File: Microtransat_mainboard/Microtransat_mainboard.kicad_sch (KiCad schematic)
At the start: 17 parts, among them IC1 HT7833, U1 LM2596S-5, U10 RC_Reciever, U5 SD Card Module, U7 LoRa Module

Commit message: Added AS5600 mockup
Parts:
- removed U7: LoRa Module, symbol Microtransat:LoRa Module
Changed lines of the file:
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@@
-		)
-	)
-	(label "RX1"
-		(at 160.02 67.31 180)
-		(effects
-			(font
-				(size 1.27 1.27)
-			)
-			(justify right bottom)
 		)
 	)
@@
 		)
 	)
-	(label "TX1"
-		(at 160.02 69.85 180)
-		(effects
-			(font
-				(size 1.27 1.27)
-			)
-			(justify right bottom)
-		)
-	)
 	(label "3V3"
 		(at 70.485 114.3 180)
@@
 			)
 			(justify left bottom)
-		)
-	)
-	(label "GND"
-		(at 160.02 64.77 180)
-		(effects
-			(font
-				(size 1.27 1.27)
-			)
-			(justify right bottom)
-		)
-	)
-	(label "5V"
-		(at 160.02 62.23 180)
-		(effects
-			(font
-				(size 1.27 1.27)
-			)
-			(justify right bottom)
 		)
 	)
@@
 					(unit 1)
 				)
-			)
-		)
-	)
-	(symbol
-		(lib_id "Microtransat:LoRa Module")
-		(at 168.275 57.15 0)
-		(unit 1)
-		(exclude_from_sim no)
-		(in_bom yes)
-		(on_board yes)
-		(dnp no)
-		(property "Reference" "U7"
-			(at 166.116 55.372 0)
-			(effects
-				(font
-					(size 1.27 1.27)
-				)
-				(justify left)
-			)
-		)
-		(property "Value" "LoRa Module"
-			(at 161.29 57.658 0)
-			(effects
-				(font
-					(size 1.27 1.27)
-				)
-				(justify left)
-			)
-		)
-		(property "Footprint" ""
-			(at 168.275 57.15 0)
-			(effects
-				(font
-					(size 1.27 1.27)
-				)
-				(hide yes)
-			)
-		)
-		(property "Datasheet" ""
-			(at 168.275 57.15 0)
-			(effects
-				(font
-					(size 1.27 1.27)
-				)
-				(hide yes)
-			)
-		)
-		(property "Description" ""
-			(at 168.275 57.15 0)
-			(effects
-				(font
-					(size 1.27 1.27)
-				)
-				(hide yes)
-			)
-		)
-		(pin "1"
-		)
-		(pin "2"
-		)
-		(pin "3"
-		)
-		(pin "4"
-		)
-		(instances
-			(project "Microtransat_mainboard"
-				(path "/89914625-be83-416e-bb0d-b792f59b4aa6"
-					(reference "U7")
-					(unit 1)
-				)

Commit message: Some adjustments
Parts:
- removed C_in1: 680 µF, symbol Device:C_Polarized
- removed C_out1: 220 µF, symbol Device:C_Polarized
- removed D3: 1N5824, Diode_THT:D_DO-201AD_P15.24mm_Horizontal, symbol Diode:1N5820
- removed L1: 33 µH, symbol Device:L
- added J1: Conn_01x03, symbol Connector_Generic:Conn_01x03
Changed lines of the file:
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@@
-	)
-	(junction
-		(at 139.7 40.64)
-		(diameter 0)
-		(color 0 0 0 0)
 	)
 	(junction
@@
 	(wire
 		(pts
-			(xy 139.7 40.64) (xy 152.4 40.64)
+			(xy 123.19 40.64) (xy 152.4 40.64)
 		)
 		(stroke
@@
 		(pts
 			(xy 68.58 43.18) (xy 68.58 40.64)
-		)
-		(stroke
-			(width 0)
-			(type default)
-		)
-	)
-	(wire
-		(pts
-			(xy 139.7 40.64) (xy 123.19 40.64)
 		)
 		(stroke
@@
 			)
 			(justify left bottom)
-		)
-	)
-	(symbol
-		(lib_id "Device:L")
-		(at 146.05 31.75 90)
-		(unit 1)
-		(exclude_from_sim no)
-		(in_bom yes)
-		(on_board yes)
-		(dnp no)
-		(fields_autoplaced yes)
-		(property "Reference" "L1"
-			(at 146.05 26.67 90)
-			(effects
-				(font
-					(size 1.27 1.27)
-				)
-			)
-		)
-		(property "Value" "33 µH"
-			(at 146.05 29.21 90)
-			(effects
-				(font
-					(size 1.27 1.27)
-				)
-			)
-		)
-		(property "Footprint" ""
-			(at 146.05 31.75 0)
-			(effects
-				(font
-					(size 1.27 1.27)
-				)
-				(hide yes)
-			)
-		)
-		(property "Datasheet" "~"
-			(at 146.05 31.75 0)
-			(effects
-				(font
-					(size 1.27 1.27)
-				)
-				(hide yes)
-			)
-		)
-		(property "Description" "Inductor"
-			(at 146.05 31.75 0)
-			(effects
-				(font
-					(size 1.27 1.27)
-				)
-				(hide yes)
-			)
-		)
-		(pin "2"
-		)
-		(pin "1"
-		)
-		(instances
-			(project "Microtransat_mainboard"
-				(path "/89914625-be83-416e-bb0d-b792f59b4aa6"
-					(reference "L1")
-					(unit 1)
-				)
-			)
-		)
-	)
-	(symbol
-		(lib_id "Diode:1N5820")
-		(at 139.7 36.83 270)
-		(unit 1)
-		(exclude_from_sim no)
-		(in_bom yes)
-		(on_board yes)
-		(dnp no)
-		(fields_autoplaced yes)
-		(property "Reference" "D3"
-			(at 142.24 35.2424 90)
-			(effects
-				(font
-					(size 1.27 1.27)
-				)
-				(justify left)
-			)
-		)
-		(property "Value" "1N5824"
-			(at 142.24 37.7824 90)
-			(effects
-				(font
-					(size 1.27 1.27)
-				)
-				(justify left)
-			)
-		)
-		(property "Footprint" "Diode_THT:D_DO-201AD_P15.24mm_Horizontal"
-			(at 135.255 36.83 0)
-			(effects
-				(font
-					(size 1.27 1.27)
-				)
-				(hide yes)
-			)
-		)
-		(property "Datasheet" "http://www.vishay.com/docs/88526/1n5820.pdf"
-			(at 139.7 36.83 0)
-			(effects
-				(font
-					(size 1.27 1.27)
-				)
-				(hide yes)
-			)
-		)
-		(property "Description" ""
-			(at 139.7 36.83 0)
-			(effects
-				(font
-					(size 1.27 1.27)
-				)
-				(hide yes)
-			)
-		)
-		(pin "1"
-		)
-		(pin "2"
-		)
-		(instances
-			(project "Microtransat_mainboard"
-				(path "/89914625-be83-416e-bb0d-b792f59b4aa6"
-					(reference "D3")
-					(unit 1)
-				)
-			)
 		)
 	)
@@
 	)
 	(symbol
+		(lib_id "Connector_Generic:Conn_01x03")
+		(at 203.2 62.23 0)
+		(unit 1)
+		(exclude_from_sim no)
+		(in_bom yes)
+		(on_board yes)
+		(dnp no)
+		(fields_autoplaced yes)
+		(property "Reference" "J1"
+			(at 205.74 60.9599 0)
+			(effects
+				(font
+					(size 1.27 1.27)
+				)
+				(justify left)
+			)
+		)
+		(property "Value" "Conn_01x03"
+			(at 205.74 63.4999 0)
+			(effects
+				(font
+					(size 1.27 1.27)
+				)
+				(justify left)
+			)
+		)
+		(property "Footprint" ""
+			(at 203.2 62.23 0)
+			(effects
+				(font
+					(size 1.27 1.27)
+				)
+				(hide yes)
+			)
+		)
+		(property "Datasheet" "~"
+			(at 203.2 62.23 0)
+			(effects
+				(font
+					(size 1.27 1.27)
+				)
+				(hide yes)
+			)
+		)
+		(property "Description" "Generic connector, single row, 01x03, script generated (kicad-library-utils/schlib/autogen/connector/)"
+			(at 203.2 62.23 0)
+			(effects
+				(font
+					(size 1.27 1.27)
+				)
+				(hide yes)
+			)
+		)
+		(pin "2"
+		)
+		(pin "1"
+		)
+		(pin "3"
+		)
+		(instances
+			(project ""
+				(path "/89914625-be83-416e-bb0d-b792f59b4aa6"
+					(reference "J1")
+					(unit 1)
+				)
+			)
+		)
+	)
+	(symbol
 		(lib_id "power:+12V")
 		(at 35.56 72.39 0)
@@
 	)
 	(symbol
-		(lib_id "Device:C_Polarized")
-		(at 104.14 33.02 0)
-		(unit 1)
-		(exclude_from_sim no)
-		(in_bom yes)
-		(on_board yes)
-		(dnp no)
-		(property "Reference" "C_in1"
-			(at 95.758 32.004 0)
-			(effects
-				(font
-					(size 1.27 1.27)
-				)
-				(justify left)
-			)
-		)
-		(property "Value" "680 µF"
-			(at 94.488 34.036 0)
-			(effects
-				(font
-					(size 1.27 1.27)
-				)
-				(justify left)
-			)
-		)
-		(property "Footprint" ""
-			(at 105.1052 36.83 0)
-			(effects
-				(font
-					(size 1.27 1.27)
-				)
-				(hide yes)
-			)
-		)
-		(property "Datasheet" "~"
-			(at 104.14 33.02 0)
-			(effects
-				(font
-					(size 1.27 1.27)
-				)
-				(hide yes)
-			)
-		)
-		(property "Description" "Polarized capacitor"
-			(at 104.14 33.02 0)
-			(effects
-				(font
-					(size 1.27 1.27)
-				)
-				(hide yes)
-			)
-		)
-		(pin "2"
-		)
-		(pin "1"
-		)
-		(instances
-			(project "Microtransat_mainboard"
-				(path "/89914625-be83-416e-bb0d-b792f59b4aa6"
-					(reference "C_in1")
-					(unit 1)
-				)
-			)
-		)
-	)
-	(symbol
 		(lib_id "Microtransat:SD Card Module")
 		(at 78.74 115.57 0)
@@
 					(unit 1)
 				)
-			)
-		)
-	)
-	(symbol
-		(lib_id "Device:C_Polarized")
-		(at 152.4 36.83 0)
-		(unit 1)
-		(exclude_from_sim no)
-		(in_bom yes)
-		(on_board yes)
-		(dnp no)
-		(property "Reference" "C_out1"
-			(at 155.702 35.814 0)
-			(effects
-				(font
-					(size 1.27 1.27)
-				)
-				(justify left)
-			)
-		)
-		(property "Value" "220 µF"
-			(at 155.702 37.846 0)
-			(effects
-				(font
-					(size 1.27 1.27)
-				)
-				(justify left)
-			)
-		)
-		(property "Footprint" ""
-			(at 153.3652 40.64 0)
-			(effects
-				(font
-					(size 1.27 1.27)
-				)
-				(hide yes)
-			)
-		)
-		(property "Datasheet" "~"
-			(at 152.4 36.83 0)
-			(effects
-				(font
-					(size 1.27 1.27)
-				)
-				(hide yes)
-			)
-		)
-		(property "Description" "Polarized capacitor"
-			(at 152.4 36.83 0)
-			(effects
-				(font
-					(size 1.27 1.27)
-				)
-				(hide yes)
-			)
-		)
-		(pin "2"
-		)
-		(pin "1"
-		)
-		(instances
-			(project "Microtransat_mainboard"
-				(path "/89914625-be83-416e-bb0d-b792f59b4aa6"
-					(reference "C_out1")
-					(unit 1)
-				)

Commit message: Moved symbol and footprint into libraries folder
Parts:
- U5: footprint (none) -> Adafruit 254:Adafruit_254
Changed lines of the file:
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@@
 			)
 		)
-		(property "Footprint" ""
+		(property "Footprint" "Adafruit 254:Adafruit_254"
 			(at 78.74 115.57 0)
 			(effects

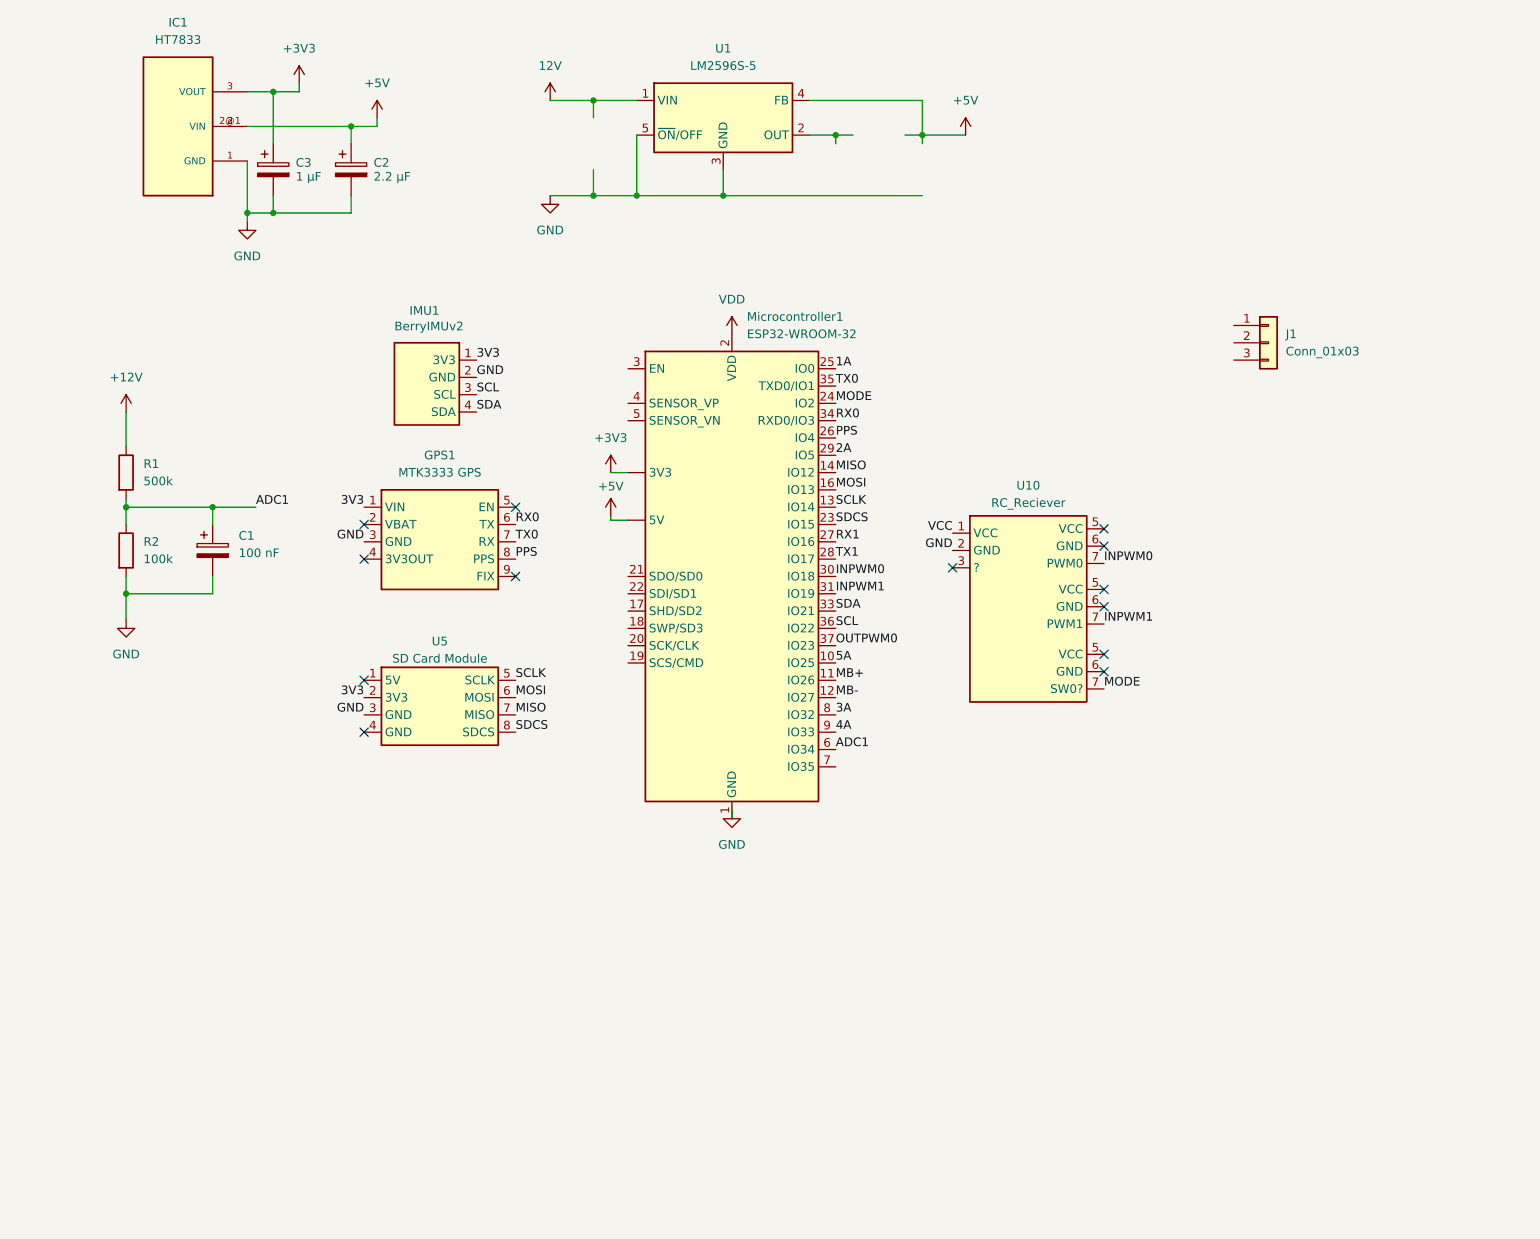
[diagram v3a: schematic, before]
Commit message: Fixed up mainboard schematic
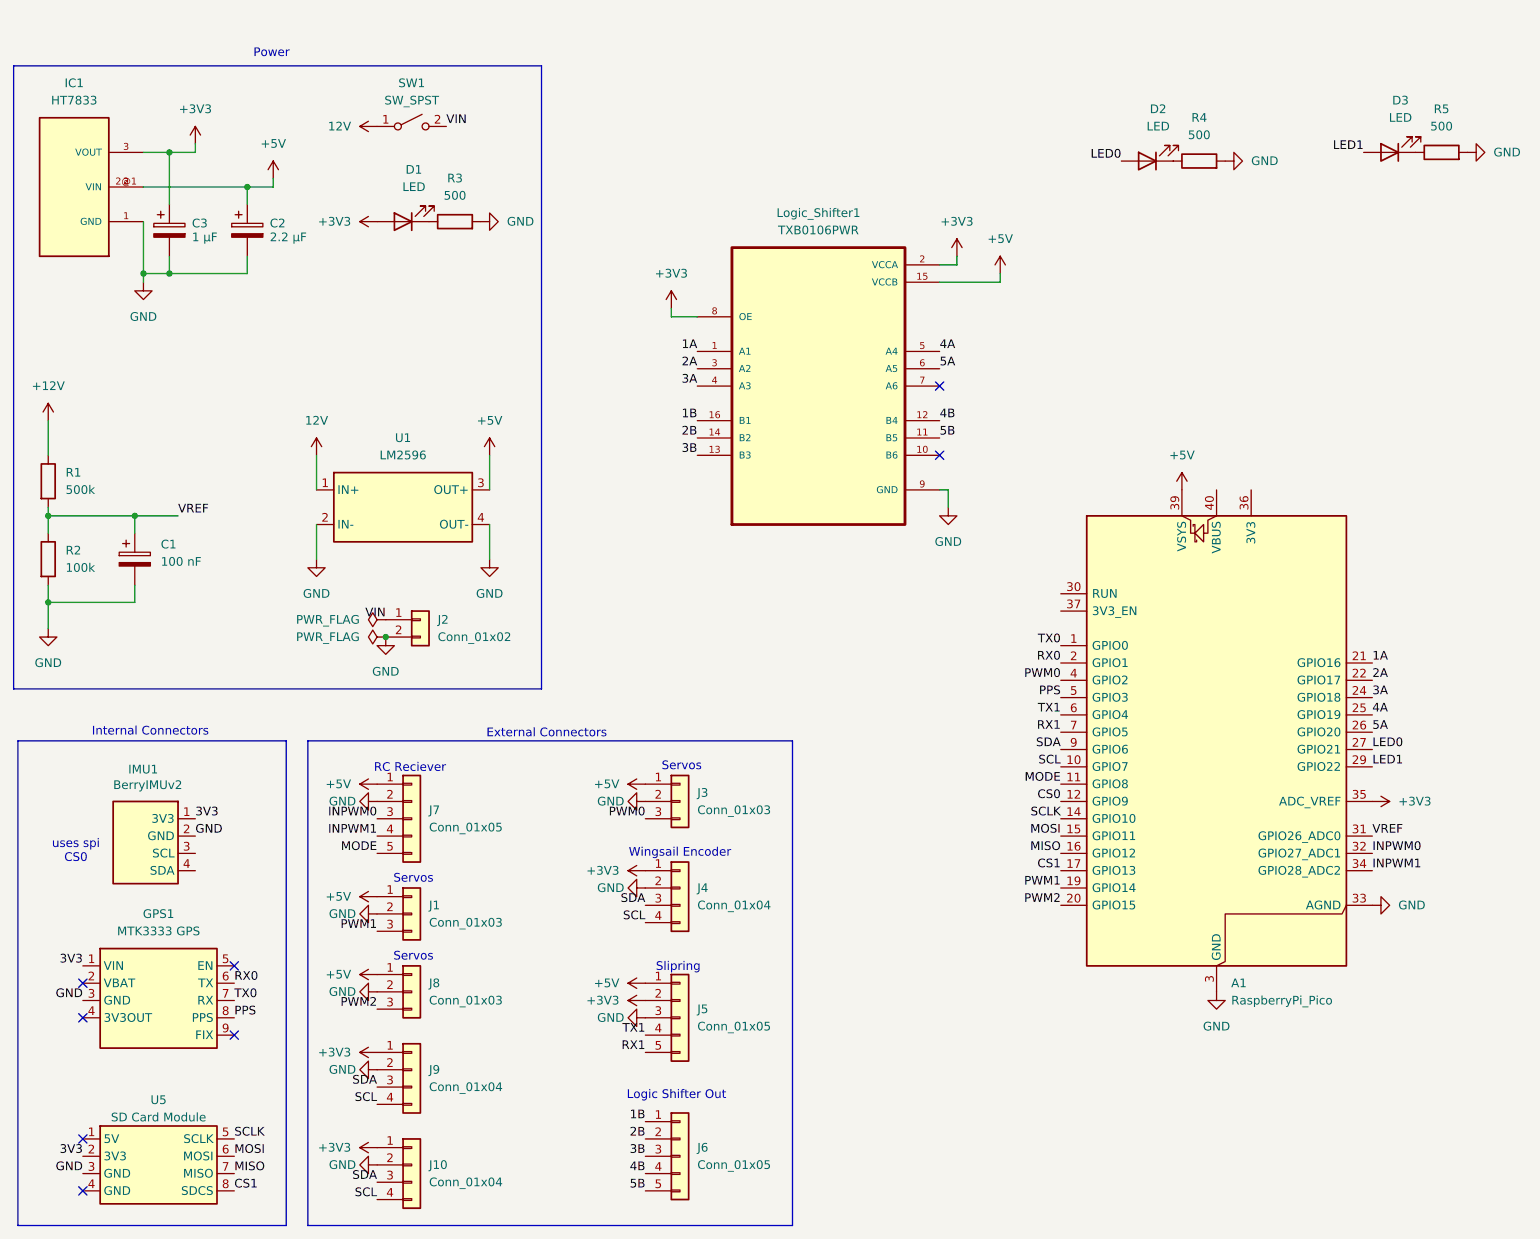
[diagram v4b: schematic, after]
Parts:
- removed Microcontroller1: ESP32-WROOM-32, RF_Module:ESP32-WROOM-32, symbol Microtransat:ESP32-WROOM-32
- removed U1: LM2596S-5, Package_TO_SOT_SMD:TO-263-5_TabPin3, symbol Regulator_Switching:LM2596S-5
- removed U10: RC_Reciever, symbol Microtransat:RC_Reciever
- added A1: RaspberryPi_Pico, Module:RaspberryPi_Pico_Common_Unspecified, symbol MCU_Module:RaspberryPi_Pico
- added D1, D2, D3: LED, symbol Device:LED
- added J10, J4, J9: Conn_01x04, symbol Connector_Generic:Conn_01x04
- added J2: Conn_01x02, symbol Connector_Generic:Conn_01x02
- added J3, J8: Conn_01x03, symbol Connector_Generic:Conn_01x03
- added J5, J6, J7: Conn_01x05, symbol Connector_Generic:Conn_01x05
- added Logic_Shifter1: TXB0106PWR, TXB0106PWR:SOP65P640X120-16N, symbol TXB0106PWR:TXB0106PWR
- added R3, R4, R5: 500, symbol Device:R
- added SW1: SW_SPST, symbol Switch:SW_SPST
- added U1: LM2596, symbol Microtransat:LM2596
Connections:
- net +3V3: now also A1.35 (ADC_VREF), D1.2 (A), J10.1 (Pin_1), J4.1 (Pin_1), J5.2 (Pin_2), J9.1 (Pin_1), Logic_Shifter1.2 (VCCA), Logic_Shifter1.8 (OE)
- net +5V: now also J1.1 (Pin_1), A1.39 (VSYS), J3.1 (Pin_1), J5.1 (Pin_1), J7.1 (Pin_1), J8.1 (Pin_1), Logic_Shifter1.15 (VCCB), U1.3 (OUT+)
- net 12V: now also SW1.1 (A), U1.1 (IN+)
- net 1A: now also A1.21 (GPIO16), Logic_Shifter1.1 (A1)
- net 2A: now also A1.22 (GPIO17), Logic_Shifter1.3 (A2)
- net 3A: now also A1.24 (GPIO18), Logic_Shifter1.4 (A3)
- net 4A: now also A1.25 (GPIO19), Logic_Shifter1.5 (A4)
- net 5A: now also A1.26 (GPIO20), Logic_Shifter1.6 (A5)
- net GND: now also J1.2 (Pin_2), A1.13 (GND), A1.18 (GND), A1.23 (GND), A1.28 (GND), A1.3 (GND), A1.33 (AGND), A1.38 (GND), A1.8 (GND), J10.2 (Pin_2), J2.2 (Pin_2), J3.2 (Pin_2), J4.2 (Pin_2), J5.3 (Pin_3), J7.2 (Pin_2), J8.2 (Pin_2), J9.2 (Pin_2), Logic_Shifter1.9 (GND), R3.2, R4.2, R5.2, U1.2 (IN-), U1.4 (OUT-)
- net INPWM0: now also A1.32 (GPIO27_ADC1), J7.3 (Pin_3)
- net INPWM1: now also A1.34 (GPIO28_ADC2), J7.4 (Pin_4)
- net MISO: now also A1.16 (GPIO12)
- net MODE: now also A1.11 (GPIO8), J7.5 (Pin_5)
- net MOSI: now also A1.15 (GPIO11)
- net PPS: now also A1.5 (GPIO3)
- net RX0: now also A1.2 (GPIO1)
- net RX1: now also A1.7 (GPIO5), J5.5 (Pin_5)
- net SCL: now also A1.10 (GPIO7), J10.4 (Pin_4), J4.4 (Pin_4), J9.4 (Pin_4); no longer IMU1.3 (SCL)
- net SCLK: now also A1.14 (GPIO10)
- net SDA: now also A1.9 (GPIO6), J10.3 (Pin_3), J4.3 (Pin_3), J9.3 (Pin_3); no longer IMU1.4 (SDA)
- net TX0: now also A1.1 (GPIO0)
- net TX1: now also A1.6 (GPIO4), J5.4 (Pin_4)
- net PWM1: now reaches J1.3 (Pin_3)
- net PWM1: now also A1.19 (GPIO14)
- net ADC1 renamed VREF
- net VREF: now also A1.31 (GPIO26_ADC0)
- net SDCS renamed CS1
- net CS1: now also A1.17 (GPIO13)
- new net: D2.1 (K), R4.1
- new net: D1.1 (K), R3.1
- new net: D3.1 (K), R5.1
- new net 1B: J6.1 (Pin_1), Logic_Shifter1.16 (B1)
- new net 2B: J6.2 (Pin_2), Logic_Shifter1.14 (B2)
- new net 3B: J6.3 (Pin_3), Logic_Shifter1.13 (B3)
- new net 4B: J6.4 (Pin_4), Logic_Shifter1.12 (B4)
- new net 5B: J6.5 (Pin_5), Logic_Shifter1.11 (B5)
- new net CS0: A1.12 (GPIO9)
- new net LED0: A1.27 (GPIO21), D2.2 (A)
- new net LED1: A1.29 (GPIO22), D3.2 (A)
- new net PWM0: A1.4 (GPIO2), J3.3 (Pin_3)
- new net PWM2: A1.20 (GPIO15), J8.3 (Pin_3)
- new net VIN: J2.1 (Pin_1), SW1.2 (B)
- no-connect marks 13 -> 8
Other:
- note added: "External Connectors"
- note added: "Internal Connectors"
- note added: "Logic Shifter Out"
- note added: "Power"
- note added: "RC Reciever"
- note added: "Servos"
- note added: "Slipring"
- note added: "Wingsail Encoder"
- note added: "uses spi CS0"
- moved on the sheet: C1, C2, C3, GPS1, IC1, IMU1, R1, R2, U5
